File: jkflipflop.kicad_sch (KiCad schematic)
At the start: 0 parts

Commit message: added decoupling caps
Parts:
- added C15: 100n, symbol Device:C
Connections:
- new net +3V3: C15.1
- new net GND: C15.2

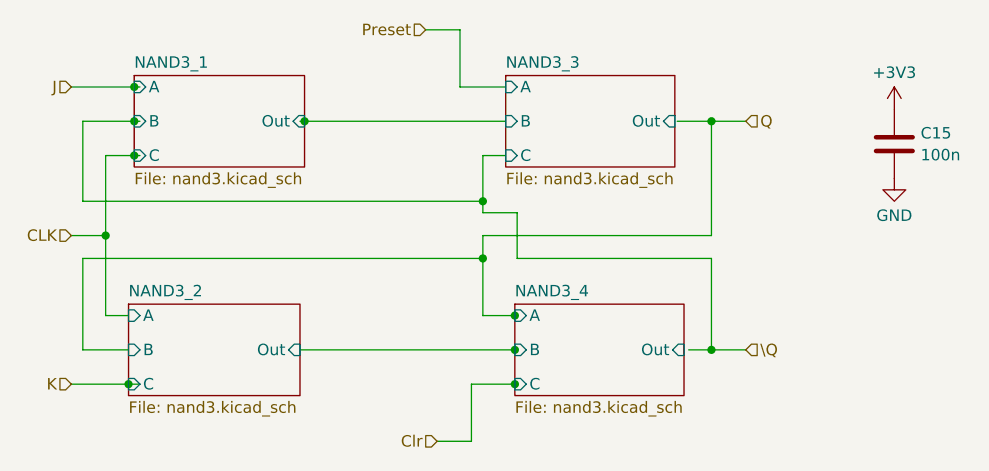
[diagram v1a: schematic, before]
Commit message: corrected output/input type of pins
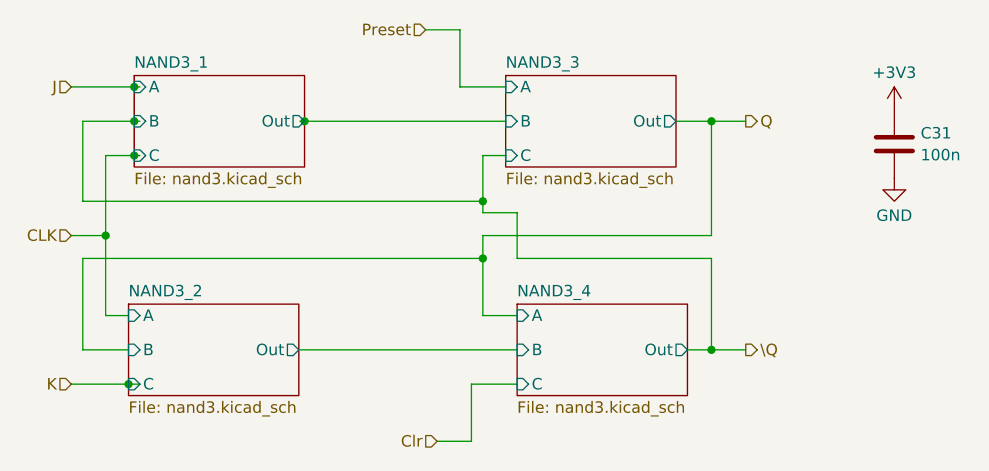
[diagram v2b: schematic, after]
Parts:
- C31: renamed from C15; footprint (none) -> Capacitor_SMD:C_0603_1608Metric

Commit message: schematic cleanup, routed 1 bdc
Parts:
- renumbered C31 to C18

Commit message: started on binary to decimal converter
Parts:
- renumbered C18 to C16

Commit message: replace bcd logic with bin-to-dec module
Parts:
- renumbered C16 to C13

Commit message: switched to using flipflop module
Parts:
- renumbered C13 to C27
